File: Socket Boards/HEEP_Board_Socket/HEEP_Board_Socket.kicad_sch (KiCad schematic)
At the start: 2 parts

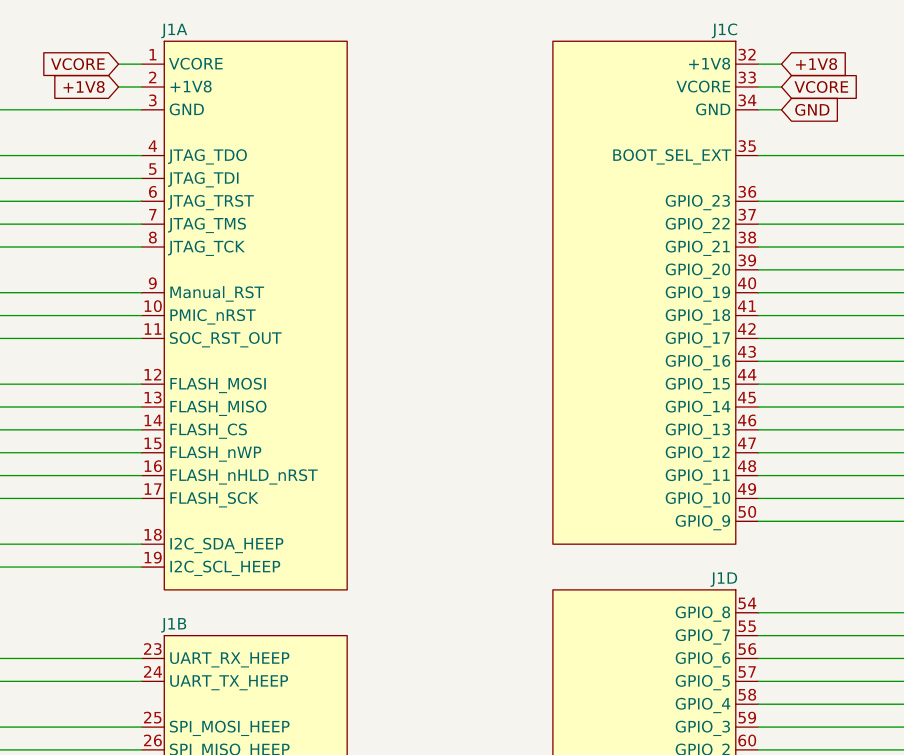
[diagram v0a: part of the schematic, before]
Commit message: Fixed paths of module boards
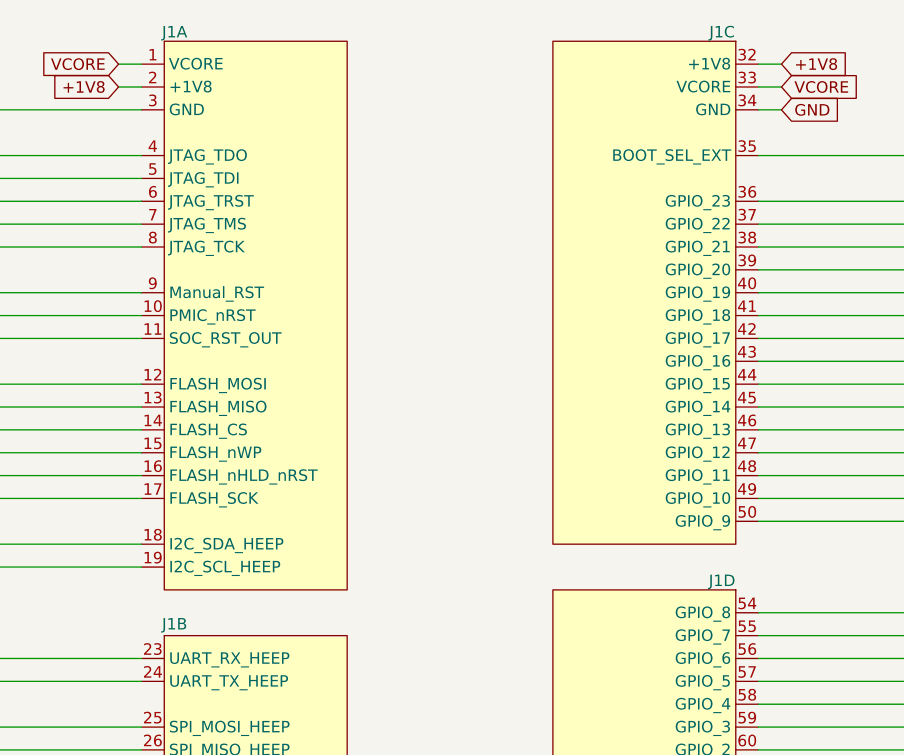
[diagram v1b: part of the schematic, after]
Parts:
- removed J1: ~, HeepoMind_PcbLib:HEEP_Board_Socket_Conn_1.27mm, symbol HeepoMind_SchLib:HEEP_Board_Socket_Conn_1.27mm
- added J1: ~, X-MODs_PcbLib:HEEP_Board_Socket_Conn_1.27mm, symbol X-MODs_SchLib:HEEP_Board_Socket_Conn_1.27mm
- J2: footprint HeepoMind_PcbLib:HEEP_Board_Header_Conn_1.27mm -> X-MODs_PcbLib:HEEP_Board_Header_Conn_1.27mm; symbol HeepoMind_SchLib:HEEP_Board_Header_Conn_1.27mm -> X-MODs_SchLib:HEEP_Board_Header_Conn_1.27mm
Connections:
- net +1V8: now also J1.2 (+1V8), J1.20 (+1V8), J1.32 (+1V8), J1.52 (+1V8)
- net GND: now also J1.22 (GND), J1.3 (GND), J1.34 (GND), J1.53 (GND)
- net VCORE: now also J1.1 (VCORE), J1.21 (VCORE), J1.33 (VCORE), J1.51 (VCORE)
- net at J2.19 (UART_RX_HEEP): now also J1.23 (UART_RX_HEEP)
- net at J2.20 (UART_TX_HEEP): now also J1.24 (UART_TX_HEEP)
- net at J2.21 (SPI_MOSI_HEEP): now also J1.25 (SPI_MOSI_HEEP)
- net at J2.22 (SPI_MISO_HEEP): now also J1.26 (SPI_MISO_HEEP)
- net at J2.23 (SPI_SD2_HEEP): now also J1.27 (SPI_SD2_HEEP)
- net at J2.24 (SPI_SD3_HEEP): now also J1.28 (SPI_SD3_HEEP)
- net at J2.25 (SPI_CS1_HEEP): now also J1.29 (SPI_CS1_HEEP)
- net at J2.26 (SPI_CS0_HEEP): now also J1.30 (SPI_CS0_HEEP)
- net at J2.27 (SPI_SCK_HEEP): now also J1.31 (SPI_SCK_HEEP)
- net at J2.28 (BOOT_SEL_EXT): now also J1.35 (BOOT_SEL_EXT)
- net at J2.29 (GPIO_23): now also J1.36 (GPIO_23)
- net at J2.30 (GPIO_22): now also J1.37 (GPIO_22)
- net at J2.31 (GPIO_21): now also J1.38 (GPIO_21)
- net at J2.32 (GPIO_20): now also J1.39 (GPIO_20)
- net at J2.33 (GPIO_19): now also J1.40 (GPIO_19)
- net at J2.34 (GPIO_18): now also J1.41 (GPIO_18)
- net at J2.35 (GPIO_17): now also J1.42 (GPIO_17)
- net at J2.36 (GPIO_16): now also J1.43 (GPIO_16)
- net at J2.37 (GPIO_15): now also J1.44 (GPIO_15)
- net at J2.38 (GPIO_14): now also J1.45 (GPIO_14)
- net at J2.39 (GPIO_13): now also J1.46 (GPIO_13)
- net at J2.40 (GPIO_12): now also J1.47 (GPIO_12)
- net at J2.41 (GPIO_11): now also J1.48 (GPIO_11)
- net at J2.42 (GPIO_10): now also J1.49 (GPIO_10)
- net at J2.43 (GPIO_9): now also J1.50 (GPIO_9)
- net at J2.44 (GPIO_8): now also J1.54 (GPIO_8)
- net at J2.45 (GPIO_7): now also J1.55 (GPIO_7)
- net at J2.46 (GPIO_6): now also J1.56 (GPIO_6)
- net at J2.47 (GPIO_5): now also J1.57 (GPIO_5)
- net at J2.48 (GPIO_4): now also J1.58 (GPIO_4)
- net at J2.49 (GPIO_3): now also J1.59 (GPIO_3)
- net at J2.50 (GPIO_2): now also J1.60 (GPIO_2)
- net at J2.51 (GPIO_1): now also J1.61 (GPIO_1)
- net at J2.52 (GPIO_0): now also J1.62 (GPIO_0)
- net at J2.9 (PMIC_nRST): now also J1.10 (PMIC_nRST)
- net at J2.10 (SOC_RST_OUT): now also J1.11 (SOC_RST_OUT)
- net at J2.11 (FLASH_MOSI): now also J1.12 (FLASH_MOSI)
- net at J2.12 (FLASH_MISO): now also J1.13 (FLASH_MISO)
- net at J2.13 (FLASH_CS): now also J1.14 (FLASH_CS)
- net at J2.14 (FLASH_nWP): now also J1.15 (FLASH_nWP)
- net at J2.15 (FLASH_nHLD_nRST): now also J1.16 (FLASH_nHLD_nRST)
- net at J2.16 (FLASH_SCK): now also J1.17 (FLASH_SCK)
- net at J2.17 (I2C_SDA_HEEP): now also J1.18 (I2C_SDA_HEEP)
- net at J2.18 (I2C_SCL_HEEP): now also J1.19 (I2C_SCL_HEEP)
- net at J2.3 (JTAG_TDO): now also J1.4 (JTAG_TDO)
- net at J2.4 (JTAG_TDI): now also J1.5 (JTAG_TDI)
- net at J2.5 (JTAG_TRST): now also J1.6 (JTAG_TRST)
- net at J2.6 (JTAG_TMS): now also J1.7 (JTAG_TMS)
- net at J2.7 (JTAG_TCK): now also J1.8 (JTAG_TCK)
- net at J2.8 (Manual_RST): now also J1.9 (Manual_RST)

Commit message: Fixed the castellated flexypins pad on the HEEP board socket
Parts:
- J1: footprint X-MODs_PcbLib:HEEP_Board_Socket_Conn_1.27mm -> X-MODs:HEEP_Board_Socket_Conn_1.27mm
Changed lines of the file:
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@@
 			)
 		)
-		(property "Footprint" "X-MODs_PcbLib:HEEP_Board_Socket_Conn_1.27mm"
+		(property "Footprint" "X-MODs:HEEP_Board_Socket_Conn_1.27mm"
 			(at 172.72 111.252 0)
 			(effects
@@
 		(property "Description" "HEEP_Board_Socket_Conn_1.27mm"
 			(at 181.61 109.22 0)
+			(effects
+				(font
+					(size 1.27 1.27)
+				)
+				(hide yes)
+			)
+		)
+		(property "MPN" ""
+			(at 179.07 43.18 0)
 			(effects
 				(font
@@
 			)
 		)
-		(property "Footprint" "X-MODs_PcbLib:HEEP_Board_Socket_Conn_1.27mm"
+		(property "Footprint" "X-MODs:HEEP_Board_Socket_Conn_1.27mm"
 			(at 121.92 111.252 0)
 			(effects
@@
 		(property "Description" "HEEP_Board_Socket_Conn_1.27mm"
 			(at 113.03 109.22 0)
+			(effects
+				(font
+					(size 1.27 1.27)
+				)
+				(hide yes)
+			)
+		)
+		(property "MPN" ""
+			(at 115.57 43.18 0)
 			(effects
 				(font
@@
 			)
 		)
-		(property "Footprint" "X-MODs_PcbLib:HEEP_Board_Socket_Conn_1.27mm"
+		(property "Footprint" "X-MODs:HEEP_Board_Socket_Conn_1.27mm"
 			(at 172.72 172.212 0)
 			(effects
@@
 		(property "Description" "HEEP_Board_Socket_Conn_1.27mm"
 			(at 181.61 170.18 0)
+			(effects
+				(font
+					(size 1.27 1.27)
+				)
+				(hide yes)
+			)
+		)
+		(property "MPN" ""
+			(at 179.07 104.14 0)
 			(effects
 				(font
@@
 			)
 		)
-		(property "Footprint" "X-MODs_PcbLib:HEEP_Board_Socket_Conn_1.27mm"
+		(property "Footprint" "X-MODs:HEEP_Board_Socket_Conn_1.27mm"
 			(at 121.92 177.292 0)
 			(effects
@@
 			(effects
 				(font
+					(size 1.27 1.27)
+				)
+				(hide yes)
+			)
+		)
+		(property "MPN" ""
+			(at 115.57 109.22 0)
+			(effects
+				(font
